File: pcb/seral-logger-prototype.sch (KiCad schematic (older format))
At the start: 38 parts

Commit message: Finish schematics (for now)
All footprints complete except on/off switch (depends on enclosure)

TODO: pin swapping for easier routing
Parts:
- removed JP?: Jumper, Connector_PinHeader_2.54mm:PinHeader_1x02_P2.54mm_Vertical, symbol Device:Jumper
- added C10, C15, C19: 10nF, Capacitor_SMD:C_0402_1005Metric, symbol Device:C_Small
- added C5: 100nF, Capacitor_SMD:C_0402_1005Metric, symbol Device:C_Small
- added J2: Conn_01x04_Female, Connector_PinSocket_2.54mm:PinSocket_1x04_P2.54mm_Vertical, symbol Connector:Conn_01x04_Female
- added R12, R13, R5, R6, R7, R8: 10k, Resistor_SMD:R_0402_1005Metric, symbol Device:R_Small
- added R2, R3, R4: 220, Resistor_SMD:R_0402_1005Metric, symbol Device:R
- added U2: 74LVC3G17, Package_SO:TSSOP-8_3x3mm_P0.65mm, symbol 74xGxx:74LVC3G17
- J1: renamed from J?; footprint (none) -> Connector_PinHeader_1.27mm:PinHeader_2x05_P1.27mm_Vertical_SMD
- L1: renamed from L?; footprint (none) -> Inductor_SMD:L_1812_4532Metric; Farnell (none) -> 2219279; MPN (none) -> LQH43PN220M26L
- R1: renamed from R?; value 270 -> 220
- SW1: renamed from SW?; footprint (none) -> Jitter_Footprints:Encoder_Switch_RGB_EC12PLRGBSDVBF
- SW2: renamed from SW?; footprint (none) -> Button_Switch_SMD:SW_SPDT_CK-JS102011SAQN
- gave numbers to parts that had none: 32
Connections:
- net labels added: A, B, CMD_DATA, SW, encoder_A, encoder_B, encoder_BTN, encoder_LED_B, encoder_LED_G, encoder_LED_R, ~OLED_CS, ~OLED_RST
- net labels removed: -BATT, CMD_DATA_256, ~CS_256, ~RST_256
- wire segments 110 -> 162
- no-connect marks 2 -> 11
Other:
- note added: "Debug UART"
- note removed: "Todo: debounce"
- moved on the sheet: SW1

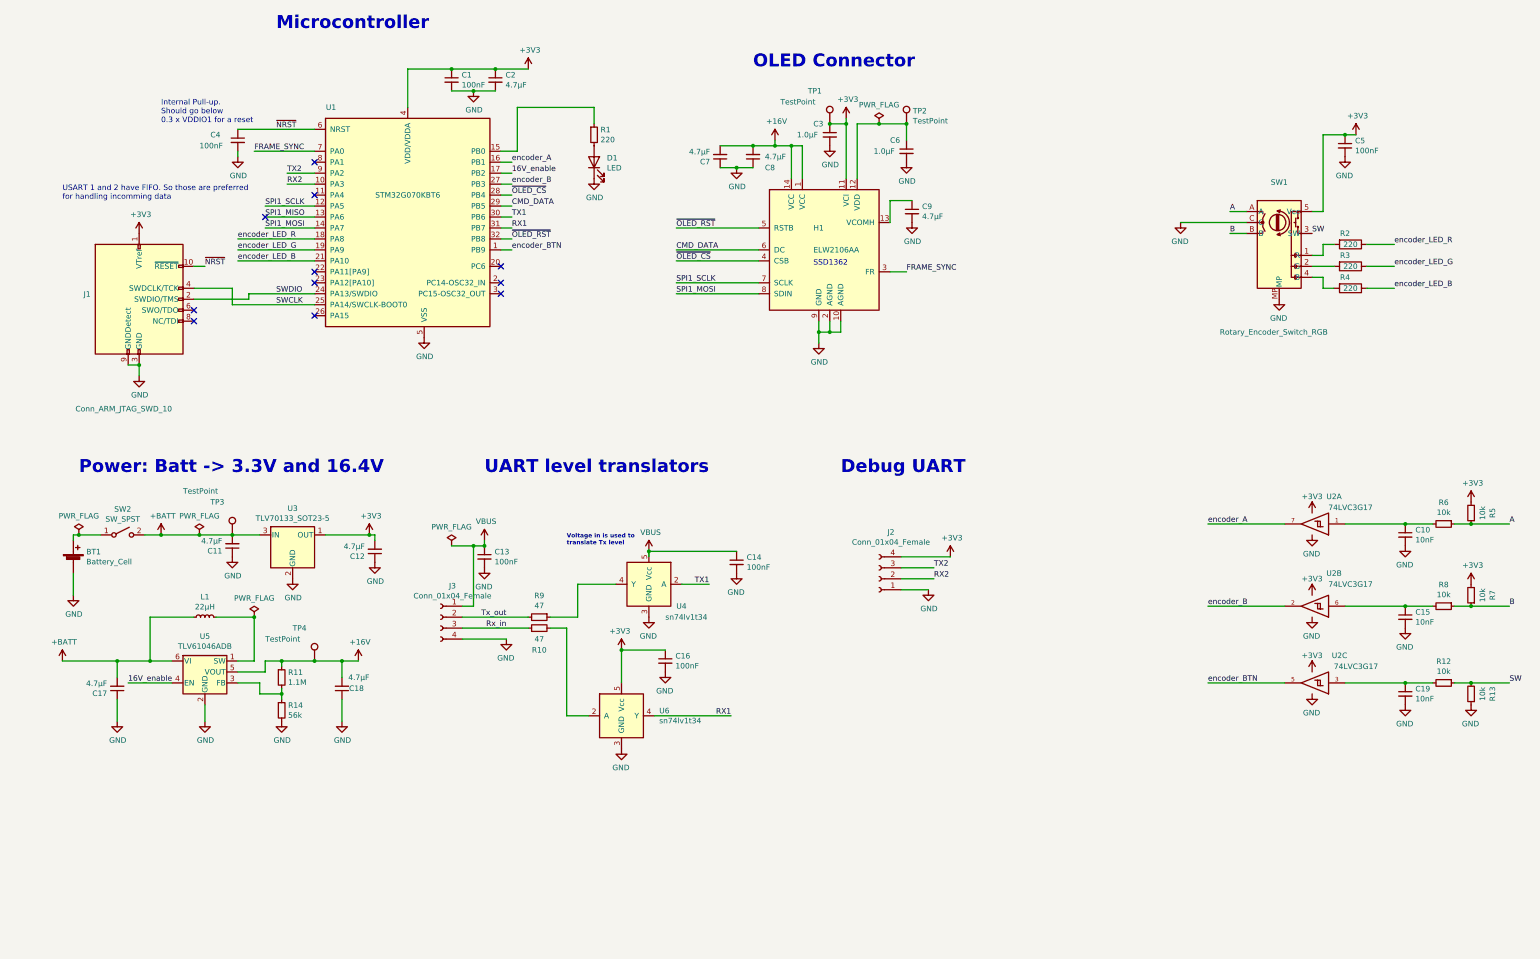
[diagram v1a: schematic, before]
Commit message: First Trial placement of components on pcb
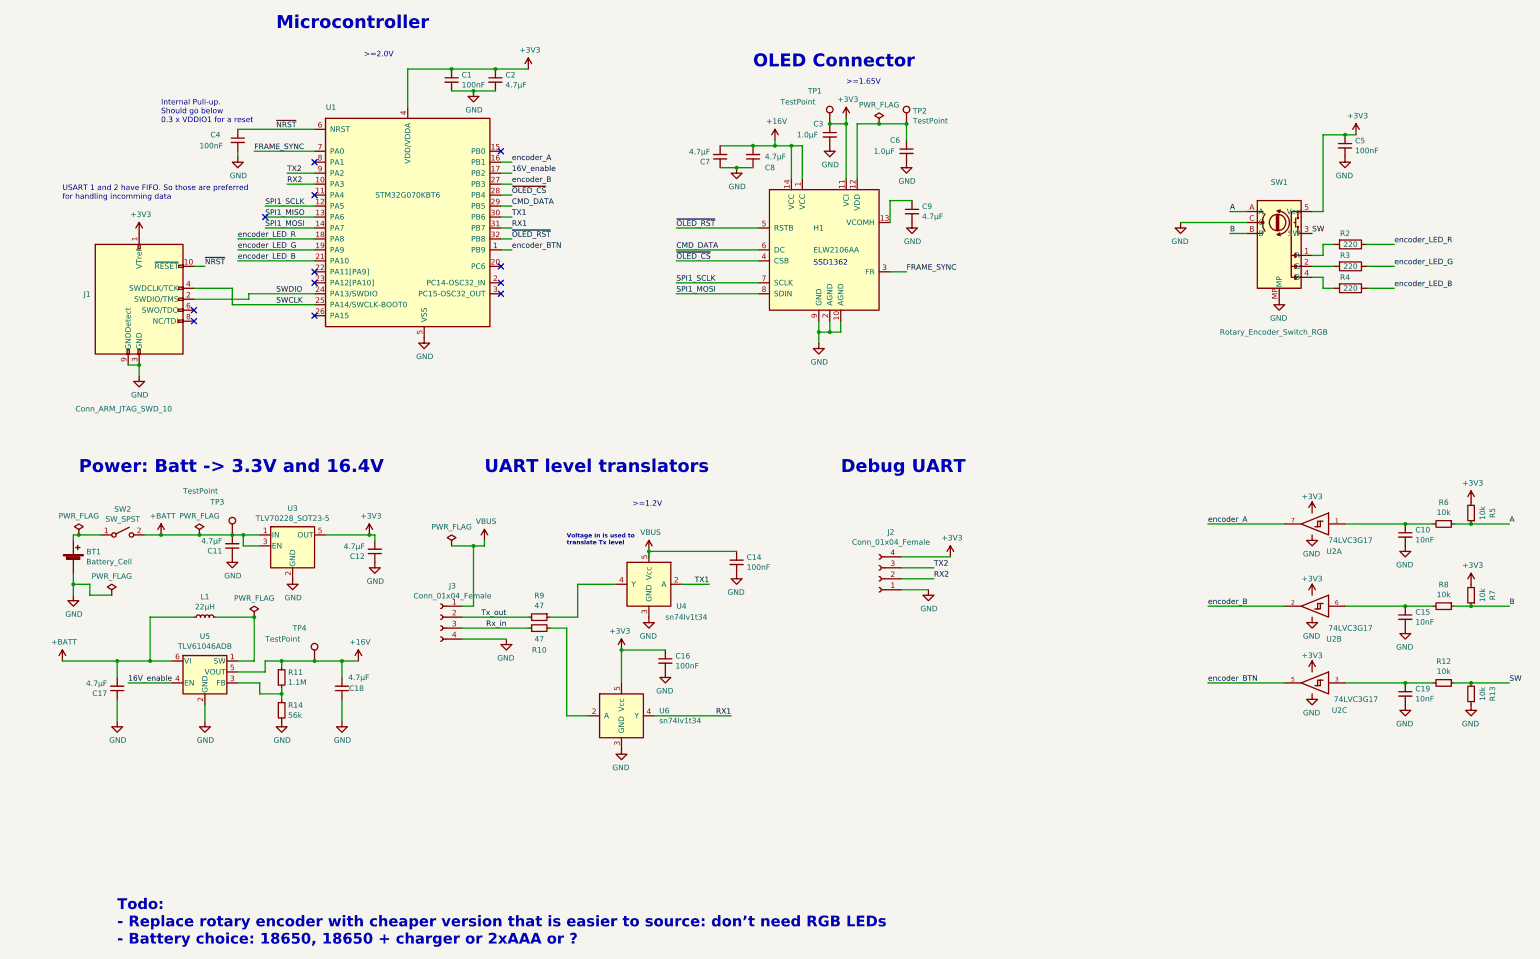
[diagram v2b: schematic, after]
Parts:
- removed C13: 100nF, Capacitor_SMD:C_0402_1005Metric, symbol Device:C_Small
- removed D1: LED, LED_SMD:LED_0603_1608Metric, symbol Device:LED
- removed R1: 220, Resistor_SMD:R_0402_1005Metric, symbol Device:R_Small
- removed U3: TLV70133_SOT23-5, Package_TO_SOT_SMD:SOT-23-5, symbol Jitter_Components:TLV70133_SOT23-5
- added U3: TLV70228_SOT23-5, Package_TO_SOT_SMD:SOT-23-5, symbol Regulator_Linear:TLV70228_SOT23-5
- TP1, TP2, TP3, TP4: footprint TestPoint:TestPoint_Plated_Hole_D3.0mm -> TestPoint:TestPoint_Plated_Hole_D2.0mm
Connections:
- net +3V3: now also U3.5 (OUT); no longer BT1.2 (-), C1.2, C10.2, C11.1, C12.1, C14.2, C15.2, C16.2, C17.1, C18.1, C19.2, C2.2, C3.2, C4.2, C5.2, C6.2, C7.1, C8.1, C9.2, H1.10 (AGND), H1.2 (AGND), H1.9 (GND), J1.3 (GND), J1.5 (GND), J1.9 (GNDDetect), J2.1 (Pin_1), J3.4 (Pin_4), R13.1, R14.2, SW1.C, SW1.MP, U1.5 (VSS), U2.4 (GND), U2.4 (GND), U2.4 (GND), U4.3 (GND), U5.2 (GND), U6.3 (GND)
- net +BATT: now also U3.1 (IN), U3.3 (EN)
- new net GND: BT1.2 (-), C1.2, C10.2, C11.1, C12.1, C14.2, C15.2, C16.2, C17.1, C18.1, C19.2, C2.2, C3.2, C4.2, C5.2, C6.2, C7.1, C8.1, C9.2, H1.10 (AGND), H1.2 (AGND), H1.9 (GND), J1.3 (GND), J1.5 (GND), J1.9 (GNDDetect), J2.1 (Pin_1), J3.4 (Pin_4), R13.1, R14.2, SW1.C, SW1.MP, U1.5 (VSS), U2.4 (GND), U2.4 (GND), U2.4 (GND), U3.2 (GND), U4.3 (GND), U5.2 (GND), U6.3 (GND)
- no-connect marks 11 -> 12
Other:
- note added: ">=1.2V"
- note added: ">=1.65V"
- note added: ">=2.0V"
- note added: "Todo:\n- Replace rotary encoder with cheaper version that is easier to source: don’t need RGB LEDs\n- Battery choice: 18650, 18650 + charger or 2xAAA or ?"

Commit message: Layout seems plausible: start routing
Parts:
- removed C5: 100nF, Capacitor_SMD:C_0402_1005Metric, symbol Device:C_Small
- removed R3, R4: 220, Resistor_SMD:R_0402_1005Metric, symbol Device:R
- removed SW1: Rotary_Encoder_Switch_RGB, Jitter_Footprints:Encoder_Switch_RGB_EC12PLRGBSDVBF, symbol Jitter_Components:Rotary_Encoder_Switch_RGB
- removed SW2: SW_SPST, Button_Switch_SMD:SW_SPDT_CK-JS102011SAQN, symbol Switch:SW_SPST
- added H2, H3: MountingHole_Pad, MountingHole:MountingHole_2.2mm_M2_Pad_Via, symbol Mechanical:MountingHole_Pad
- added R1: 220, Resistor_SMD:R_0402_1005Metric, symbol Device:R
- added SW1: Rotary_Encoder_Switch_DualLED, Jitter_Footprints:PEL12D-4xxxS-Sxxxx, symbol Jitter_Components:Rotary_Encoder_Switch_DualLED
- added SW2: SW_SPDT, Jitter_Footprints:slide_switch_09.03201.02, symbol Switch:SW_SPDT
- BT1: footprint Jitter_Footprints:BatteryHolder_Keystone_1042(P)__1043(P)_1x18650 -> Jitter_Footprints:BatteryHolder_Keystone_1043(p)_1x18650
- R13, R5, R7: footprint Resistor_SMD:R_0402_1005Metric -> Resistor_SMD:R_0603_1608Metric
- TP1, TP2, TP3, TP4: footprint TestPoint:TestPoint_Plated_Hole_D2.0mm -> TestPoint:TestPoint_Pad_D1.5mm
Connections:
- net +3V3: now also R13.2
- net +BATT: now also SW2.2 (B)
- net A: now also R12.1, R13.1, SW1.A; no longer R5.1, R6.1
- net B: now also R5.1, R6.1, SW1.B; no longer R7.1, R8.1
- net GND: now also H2.1, H3.1, SW1.1 (GND), SW1.C, SW1.MP; no longer R13.1
- net SW: now also R7.1, R8.1, SW1.4 (SW); no longer R12.1, R13.2
- net encoder_A: now also U2.5; no longer U2.7
- net encoder_B: now also U2.7; no longer U2.2
- net encoder_BTN: now also U2.2; no longer U2.5
- net encoder_LED_G: now also R1.1
- net at BT1.1 (+): now also SW2.1 (A)
- net at R2.2: now also SW1.3 (LED2)
- new net: R1.2, SW1.2 (LED1)
- no-connect marks 12 -> 13
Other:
- note added: "Todo:\n- Battery choice: 18650, 18650 + charger or 2xAAA or ?\n- Select right angle slide switch for on/off"
- note removed: "Todo:\n- Replace rotary encoder with cheaper version that is easier to source: don’t need RGB LEDs\n- Battery choice: 18650, 18650 + charger or 2xAAA or ?"
- moved on the sheet: BT1, R13

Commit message: Finish routing and pin swapping
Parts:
- removed TP1, TP2: TestPoint, TestPoint:TestPoint_Pad_D1.5mm, symbol Connector:TestPoint
- added C5: 10nF, Capacitor_SMD:C_0402_1005Metric, symbol Device:C_Small
- added J4: Conn_01x03_Male, Connector_PinHeader_2.54mm:PinHeader_1x03_P2.54mm_Vertical, symbol Connector:Conn_01x03_Male
- added R3, R4: 47, Resistor_SMD:R_0402_1005Metric, symbol Device:R_Small
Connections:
- net encoder_LED_B is gone; now on net RX1: U1.21 (PA10)
- net +3V3: now also C5.1
- net +BATT: now also R3.2
- net 16V_enable: now also U1.8 (PA1); no longer U1.17 (PB2)
- net CMD_DATA: now also U1.31 (PB7); no longer U1.29 (PB5)
- net FRAME_SYNC: now also U1.26 (PA15); no longer U1.7 (PA0)
- net GND: now also C5.2, J4.3 (Pin_3), R4.1
- net RX1: no longer U1.31 (PB7)
- net RX2: no longer J2.2 (Pin_2)
- net SPI1_MOSI: now also U1.29 (PB5); no longer U1.14 (PA7)
- net SPI1_SCLK: now also U1.27 (PB3); no longer U1.12 (PA5)
- net TX1: now also U1.19 (PA9); no longer U1.30 (PB6)
- net TX2: no longer J2.3 (Pin_3)
- net encoder_B: now also U1.17 (PB2); no longer U1.27 (PB3)
- net encoder_BTN: now also U1.18 (PA8); no longer U1.1 (PB9)
- net encoder_LED_G: now also U1.14 (PA7); no longer U1.19 (PA9)
- net encoder_LED_R: now also U1.15 (PB0); no longer U1.18 (PA8)
- net ~OLED_RST: now also U1.30 (PB6); no longer U1.32 (PB8)
- net BAT_VOLT: now reaches U1.11 (PA4)
- net BAT_VOLT: now also R3.1, R4.2
- net PA11: now reaches U1.22 (PA11[PA9])
- net PA11: now also J4.1 (Pin_1)
- net PA12: now reaches U1.23 (PA12[PA10])
- net PA12: now also J4.2 (Pin_2)
- net SPI1_MISO: no longer names the net of U1.13 (PA6)
- new net DEBUG_RX3: J2.2 (Pin_2), U1.1 (PB9)
- new net DEBUG_TX3: J2.3 (Pin_3), U1.32 (PB8)
- no-connect marks 13 -> 11
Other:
- note added: "NRST has Internal Pull-up. \nShould go below \n0.3 x VDDIO1 for a reset"
- note added: "TODO: resister divider"
- note added: "USART 1 and 2 have FIFO. \nSo those are preferred for \nhandling incomming data"
- note removed: "Internal Pull-up. \nShould go below \n0.3 x VDDIO1 for a reset"
- note removed: "Todo:\n- Battery choice: 18650, 18650 + charger or 2xAAA or ?\n- Select right angle slide switch for on/off"
- note removed: "USART 1 and 2 have FIFO. So those are preferred \nfor handling incomming data"
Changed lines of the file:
@@
 Comment4 ""
 $EndDescr
-Text Notes 800  2400 0    50   ~ 0
-USART 1 and 2 have FIFO. So those are preferred \nfor handling incomming data
+Text Notes 750  2250 0    50   ~ 0
+USART 1 and 2 have FIFO. \nSo those are preferred for \nhandling incomming data
 Text Label 2850 2250 0    50   ~ 0
 RX2
 Text Label 2850 2150 0    50   ~ 0
 TX2
-Text Label 4900 2550 0    50   ~ 0
+Text Label 2850 2850 0    50   ~ 0
 TX1
-Text Label 4900 2650 0    50   ~ 0
+Text Label 2850 2950 0    50   ~ 0
 RX1
 Wire Wire Line
@@
 $EndComp
 Text Notes 1700 1700 0    50   ~ 0
-Internal Pull-up. \nShould go below \n0.3 x VDDIO1 for a reset
-Text Label 2650 2550 0    50   ~ 0
-SPI1_MISO
-Text Label 2650 2650 0    50   ~ 0
+NRST has Internal Pull-up. \nShould go below \n0.3 x VDDIO1 for a reset
+Text Label 4900 2450 0    50   ~ 0
 SPI1_MOSI
 Wire Wire Line
 	2650 2550 3100 2550
-Wire Wire Line
-	3100 2650 2650 2650
 $Comp
 L Device:C_Small C4
@@
 	1    0    0    -1
 $EndComp
-$Comp
-L Connector:TestPoint TP2
-U 1 1 5E1A29F6
-P 8500 1700
-F 0 "TP2" H 8558 1818 50  0000 L CNN
-F 1 "TestPoint" H 8558 1727 50  0000 L CNN
-F 2 "TestPoint:TestPoint_Pad_D1.5mm" H 8700 1700 50  0001 C CNN
-F 3 "~" H 8700 1700 50  0001 C CNN
-	1    8500 1700
-	1    0    0    -1
-$EndComp
-Connection ~ 8500 1700
-$Comp
-L Connector:TestPoint TP1
-U 1 1 5E1A34F1
-P 7800 1700
-F 0 "TP1" H 7600 2000 50  0000 L CNN
-F 1 "TestPoint" H 7350 1900 50  0000 L CNN
-F 2 "TestPoint:TestPoint_Pad_D1.5mm" H 8000 1700 50  0001 C CNN
-F 3 "~" H 8000 1700 50  0001 C CNN
-	1    7800 1700
-	1    0    0    -1
-$EndComp
-Connection ~ 7800 1700
 $Comp
 L Jitter_Components:+16V #PWR05
@@
 Text Label 6400 3250 0    50   ~ 0
 SPI1_MOSI
-Text Label 2650 2450 0    50   ~ 0
+Text Label 4900 2250 0    50   ~ 0
 SPI1_SCLK
-Wire Wire Line
-	2650 2450 3100 2450
 Text Label 6400 3150 0    50   ~ 0
 SPI1_SCLK
@@
 Wire Wire Line
 	8500 3050 8350 3050
-Text Label 2550 1950 0    50   ~ 0
+Text Label 2550 3450 0    50   ~ 0
 FRAME_SYNC
-Wire Wire Line
-	2550 1950 3100 1950
 $Comp
 L Device:Battery_Cell BT1
@@
 Wire Wire Line
 	1400 6800 1800 6800
-Text Label 4900 2150 0    50   ~ 0
+Text Label 2550 2050 0    50   ~ 0
 16V_enable
 Wire Wire Line
@@
 F 0 "TP3" H 2150 5750 50  0000 L CNN
 F 1 "TestPoint" H 1900 5850 50  0000 L CNN
-F 2 "TestPoint:TestPoint_Pad_D1.5mm" H 2550 5450 50  0000 C CNN
+F 2 "TestPoint:TestPoint_Pad_D1.5mm" H 2900 5850 50  0001 C CNN
 F 3 "~" H 2550 5450 50  0001 C CNN
 	1    2350 5450
@@
 Text Notes 5400 5550 0    39   ~ 8
 Voltage in is used to \ntranslate Tx level
-NoConn ~ 3100 2050
-NoConn ~ 3100 2350
-NoConn ~ 3100 3050
-NoConn ~ 3100 3150
 NoConn ~ 4800 3000
 NoConn ~ 4800 3150
@@
 Wire Wire Line
 	8700 5950 8450 5950
-Text Label 8750 5750 0    50   ~ 0
-TX2
 Wire Wire Line
 	8750 5750 8450 5750
-Text Label 8750 5850 0    50   ~ 0
-RX2
 Wire Wire Line
 	8750 5850 8450 5850
 Wire Wire Line
 	2400 1950 2400 2000
-NoConn ~ 3100 3450
 NoConn ~ 2650 2550
 $Comp
@@
 	4350 5550 4550 5550
 Connection ~ 4550 5550
-Text Label 4900 2750 0    50   ~ 0
+Text Label 4900 2550 0    50   ~ 0
 ~OLED_RST
 Text Label 4900 2350 0    50   ~ 0
@@
 Wire Wire Line
 	4900 2350 4800 2350
-Text Label 4900 2450 0    50   ~ 0
-CMD_DATA
 Wire Wire Line
 	4800 2450 4900 2450
-Text Label 2400 2750 0    50   ~ 0
+Text Label 4900 1950 0    50   ~ 0
 encoder_LED_R
-Text Label 2400 2850 0    50   ~ 0
+Text Label 2400 2650 0    50   ~ 0
 encoder_LED_G
-Text Label 2400 2950 0    50   ~ 0
-encoder_LED_B
 $Comp
 L Jitter_Components:STM32G070KBT6 U1
@@
 	2400 2750 3100 2750
 Wire Wire Line
-	3100 2850 2400 2850
-Wire Wire Line
-	2400 2950 3100 2950
+	3100 2850 2850 2850
 Text Label 4900 2050 0    50   ~ 0
 encoder_A
 Wire Wire Line
 	4800 2050 4900 2050
-Text Label 4900 2250 0    50   ~ 0
+Text Label 4900 2150 0    50   ~ 0
 encoder_B
-Text Label 4900 2850 0    50   ~ 0
+Text Label 2400 2750 0    50   ~ 0
 encoder_BTN
 Wire Wire Line
@@
 Wire Wire Line
 	2450 5450 2600 5450
-Text Notes 1300 9200 0    98   ~ 20
-Todo:\n- Battery choice: 18650, 18650 + charger or 2xAAA or ?\n- Select right angle slide switch for on/off
-NoConn ~ 4800 1950
 Wire Wire Line
 	13100 3350 13000 3350
@@
 	1    0    0    -1
 $EndComp
+$Comp
+L Device:C_Small C5
+U 1 1 5E221970
+P 12600 4900
+F 0 "C5" H 12692 4946 50  0000 L CNN
+F 1 "10nF" H 12692 4855 50  0000 L CNN
+F 2 "Capacitor_SMD:C_0402_1005Metric" H 12600 4900 50  0001 C CNN
+F 3 "~" H 12600 4900 50  0001 C CNN
+	1    12600 4900
+	1    0    0    -1
+$EndComp
+$Comp
+L power:GND #PWR013
+U 1 1 5E221E67
+P 12600 5000
+F 0 "#PWR013" H 12600 4750 50  0001 C CNN
+F 1 "GND" H 12605 4827 50  0000 C CNN
+F 2 "" H 12600 5000 50  0001 C CNN
+F 3 "" H 12600 5000 50  0001 C CNN
+	1    12600 5000
+	-1   0    0    -1
+$EndComp
+$Comp
+L power:+3V3 #PWR011
+U 1 1 5E2222EE
+P 12600 4800
+F 0 "#PWR011" H 12600 4650 50  0001 C CNN
+F 1 "+3V3" H 12600 4950 50  0000 C CNN
+F 2 "" H 12600 4800 50  0001 C CNN
+F 3 "" H 12600 4800 50  0001 C CNN
+	1    12600 4800
+	1    0    0    -1
+$EndComp
+Text Label 5600 1450 0    50   ~ 0
+BAT_VOLT
+$Comp
+L Device:R_Small R3
+U 1 1 5E268A33
+P 6450 1200
+F 0 "R3" V 6254 1200 50  0000 C CNN
+F 1 "47" V 6345 1200 50  0000 C CNN
+F 2 "Resistor_SMD:R_0402_1005Metric" H 6450 1200 50  0001 C CNN
+F 3 "~" H 6450 1200 50  0001 C CNN
+	1    6450 1200
+	-1   0    0    1
+$EndComp
+$Comp
+L Device:R_Small R4
+U 1 1 5E269799
+P 6450 1500
+F 0 "R4" V 6254 1500 50  0000 C CNN
+F 1 "47" V 6345 1500 50  0000 C CNN
+F 2 "Resistor_SMD:R_0402_1005Metric" H 6450 1500 50  0001 C CNN
+F 3 "~" H 6450 1500 50  0001 C CNN
+	1    6450 1500
+	-1   0    0    1
+$EndComp
+Wire Wire Line
+	6450 1300 6450 1350
+$Comp
+L power:GND #PWR030
+U 1 1 5E272F3E
+P 6450 1600
+F 0 "#PWR030" H 6450 1350 50  0001 C CNN
+F 1 "GND" H 6455 1427 50  0000 C CNN
+F 2 "" H 6450 1600 50  0001 C CNN
+F 3 "" H 6450 1600 50  0001 C CNN
+	1    6450 1600
+	1    0    0    -1
+$EndComp
+Wire Wire Line
+	6250 1450 6250 1350
+Wire Wire Line
+	6250 1350 6450 1350
+Wire Wire Line
+	5600 1450 6250 1450
+Connection ~ 6450 1350
+Wire Wire Line
+	6450 1350 6450 1400
+$Comp
+L power:+BATT #PWR015
+U 1 1 5E27CB82
+P 6450 1100
+F 0 "#PWR015" H 6450 950 50  0001 C CNN
+F 1 "+BATT" H 6465 1273 50  0000 C CNN
+F 2 "" H 6450 1100 50  0001 C CNN
+F 3 "" H 6450 1100 50  0001 C CNN
+	1    6450 1100
+	1    0    0    -1
+$EndComp
+Text Notes 6200 850  0    50   ~ 0
+TODO: resister divider
+Wire Wire Line
+	2550 3450 3100 3450
+Text Label 4900 2650 0    50   ~ 0
+CMD_DATA
+Wire Wire Line
+	2850 2950 3100 2950
+Wire Wire Line
+	4900 1950 4800 1950
+Wire Wire Line
+	2400 2650 3100 2650
+Text Label 4900 2750 0    50   ~ 0
+DEBUG_TX3
+Text Label 4900 2850 0    50   ~ 0
+DEBUG_RX3
+Text Label 8750 5750 0    50   ~ 0
+DEBUG_TX3
+Text Label 8750 5850 0    50   ~ 0
+DEBUG_RX3
+Wire Wire Line
+	2550 2050 3100 2050
+Text Label 2650 2350 0    50   ~ 0
+BAT_VOLT
+Wire Wire Line
+	3100 2350 2650 2350
+NoConn ~ 3100 2450
+NoConn ~ 3100 1950
+$Comp
+L Connector:Conn_01x03_Male J4
+U 1 1 5E4ED10B
+P 3900 4250
+F 0 "J4" H 3872 4274 50  0000 R CNN
+F 1 "Conn_01x03_Male" H 3872 4183 50  0000 R CNN
+F 2 "Connector_PinHeader_2.54mm:PinHeader_1x03_P2.54mm_Vertical" H 3900 4250 50  0001 C CNN
+F 3 "~" H 3900 4250 50  0001 C CNN
+	1    3900 4250
+	-1   0    0    -1
+$EndComp
+Text Label 2850 3150 0    50   ~ 0
+PA12
+Text Label 2850 3050 0    50   ~ 0
+PA11
+Wire Wire Line
+	2850 3050 3100 3050
+Wire Wire Line
+	3100 3150 2850 3150
+Text Label 3450 4250 0    50   ~ 0
+PA12
+Text Label 3450 4150 0    50   ~ 0
+PA11
+Wire Wire Line
+	3450 4150 3700 4150
+Wire Wire Line
+	3700 4250 3450 4250
+$Comp
+L power:GND #PWR0105
+U 1 1 5E517EBE
+P 3450 4350
+F 0 "#PWR0105" H 3450 4100 50  0001 C CNN
+F 1 "GND" H 3455 4177 50  0000 C CNN
+F 2 "" H 3450 4350 50  0001 C CNN
+F 3 "" H 3450 4350 50  0001 C CNN
+	1    3450 4350
+	1    0    0    -1
+$EndComp
+Wire Wire Line
+	3450 4350 3700 4350
+NoConn ~ 2850 2150
+NoConn ~ 2850 2250
 $EndSCHEMATC
